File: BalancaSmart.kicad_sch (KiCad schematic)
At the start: 54 parts, among them J1 Load Cell, J2 Barrel_Jack, Q1 PMOS, Q2 NMOS, Q3 NMOS, Q4 S8050, SW1 SW_Push, U1 HX711-Mod, U2 ADS1115-module, U3 HX-2S-JH20, U4 XL4015

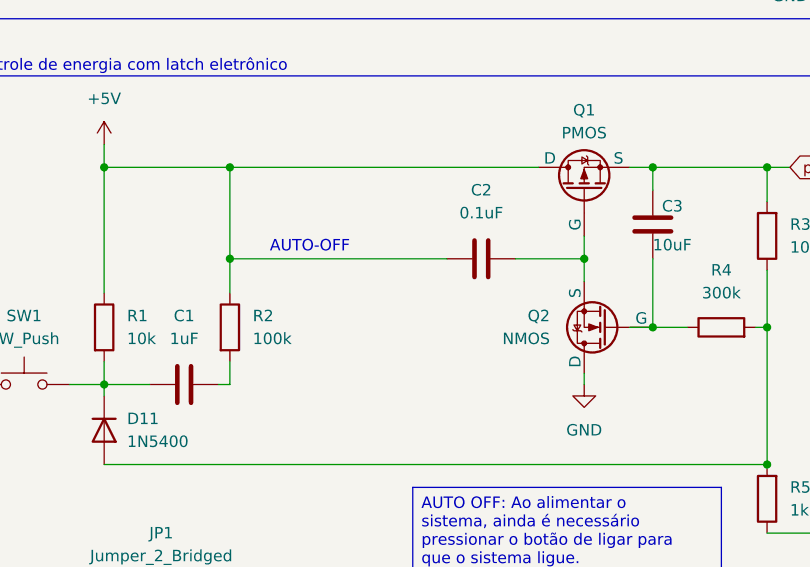
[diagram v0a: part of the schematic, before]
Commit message: correção na ligação do circuito de latch
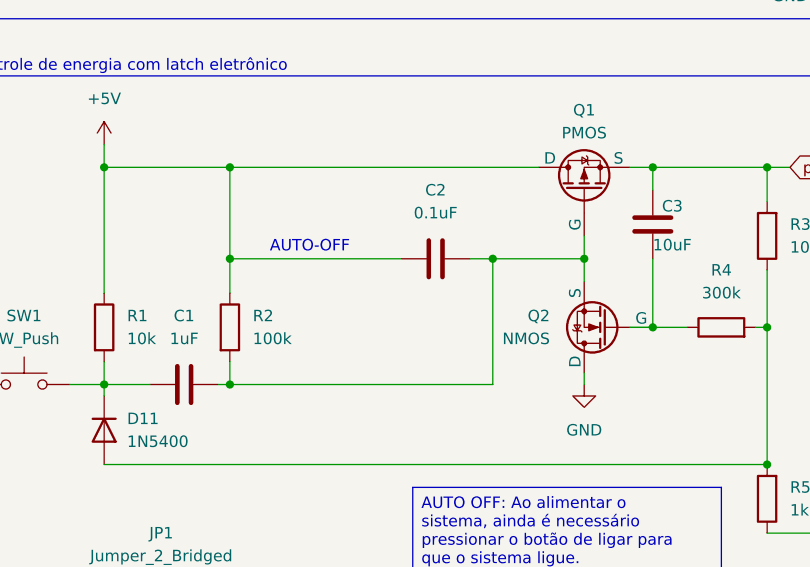
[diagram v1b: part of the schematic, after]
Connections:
- net at C2.2, Q1.2 (G), Q2.3 (S): now also C1.2, R2.2
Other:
- moved on the sheet: C2
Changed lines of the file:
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@@
 	)
 	(junction
+		(at 45.72 163.83)
+		(diameter 0)
+		(color 0 0 0 0)
+	)
+	(junction
 		(at 68.58 78.74)
 		(diameter 0)
@@
 	)
 	(junction
+		(at 74.93 149.86)
+		(diameter 0)
+		(color 0 0 0 0)
+	)
+	(junction
 		(at 200.66 27.94)
 		(diameter 0)
@@
 	(wire
 		(pts
+			(xy 45.72 163.83) (xy 74.93 163.83)
+		)
+		(stroke
+			(width 0)
+			(type default)
+		)
+	)
+	(wire
+		(pts
 			(xy 215.9 156.21) (xy 215.9 157.48)
 		)
@@
 	(wire
 		(pts
-			(xy 45.72 149.86) (xy 69.85 149.86)
+			(xy 45.72 149.86) (xy 64.77 149.86)
 		)
 		(stroke
@@
 	(wire
 		(pts
-			(xy 77.47 149.86) (xy 85.09 149.86)
-		)
-		(stroke
-			(width 0)
-			(type default)
-		)
-	)
-	(wire
-		(pts
 			(xy 219.71 41.91) (xy 219.71 46.99)
 		)
@@
 	(wire
 		(pts
+			(xy 72.39 149.86) (xy 74.93 149.86)
+		)
+		(stroke
+			(width 0)
+			(type default)
+		)
+	)
+	(wire
+		(pts
 			(xy 257.81 54.61) (xy 257.81 57.15)
 		)
@@
 	(wire
 		(pts
+			(xy 74.93 149.86) (xy 85.09 149.86)
+		)
+		(stroke
+			(width 0)
+			(type default)
+		)
+	)
+	(wire
+		(pts
 			(xy 250.19 57.15) (xy 257.81 57.15)
 		)
@@
 	(wire
 		(pts
+			(xy 74.93 163.83) (xy 74.93 149.86)
+		)
+		(stroke
+			(width 0)
+			(type default)
+		)
+	)
+	(wire
+		(pts
 			(xy 45.72 100.33) (xy 53.34 100.33)
 		)
@@
 	(symbol
 		(lib_id "Device:C")
-		(at 73.66 149.86 90)
+		(at 68.58 149.86 90)
 		(unit 1)
 		(body_style 1)
@@
 		(fields_autoplaced yes)
 		(property "Reference" "C2"
-			(at 73.66 142.24 90)
+			(at 68.58 142.24 90)
 			(show_name no)
 			(do_not_autoplace no)
@@
 		)
 		(property "Value" "0.1uF"
-			(at 73.66 144.78 90)
+			(at 68.58 144.78 90)
 			(show_name no)
 			(do_not_autoplace no)
@@
 		)
 		(property "Footprint" "Capacitor_THT:C_Disc_D5.0mm_W2.5mm_P2.50mm"
-			(at 77.47 148.8948 0)
+			(at 72.39 148.8948 0)
 			(hide yes)
 			(show_name no)
@@
 		)
 		(property "Datasheet" ""
-			(at 73.66 149.86 0)
+			(at 68.58 149.86 0)
 			(hide yes)
 			(show_name no)
@@
 		)
 		(property "Description" "Unpolarized capacitor"
-			(at 73.66 149.86 0)
+			(at 68.58 149.86 0)
 			(hide yes)
 			(show_name no)

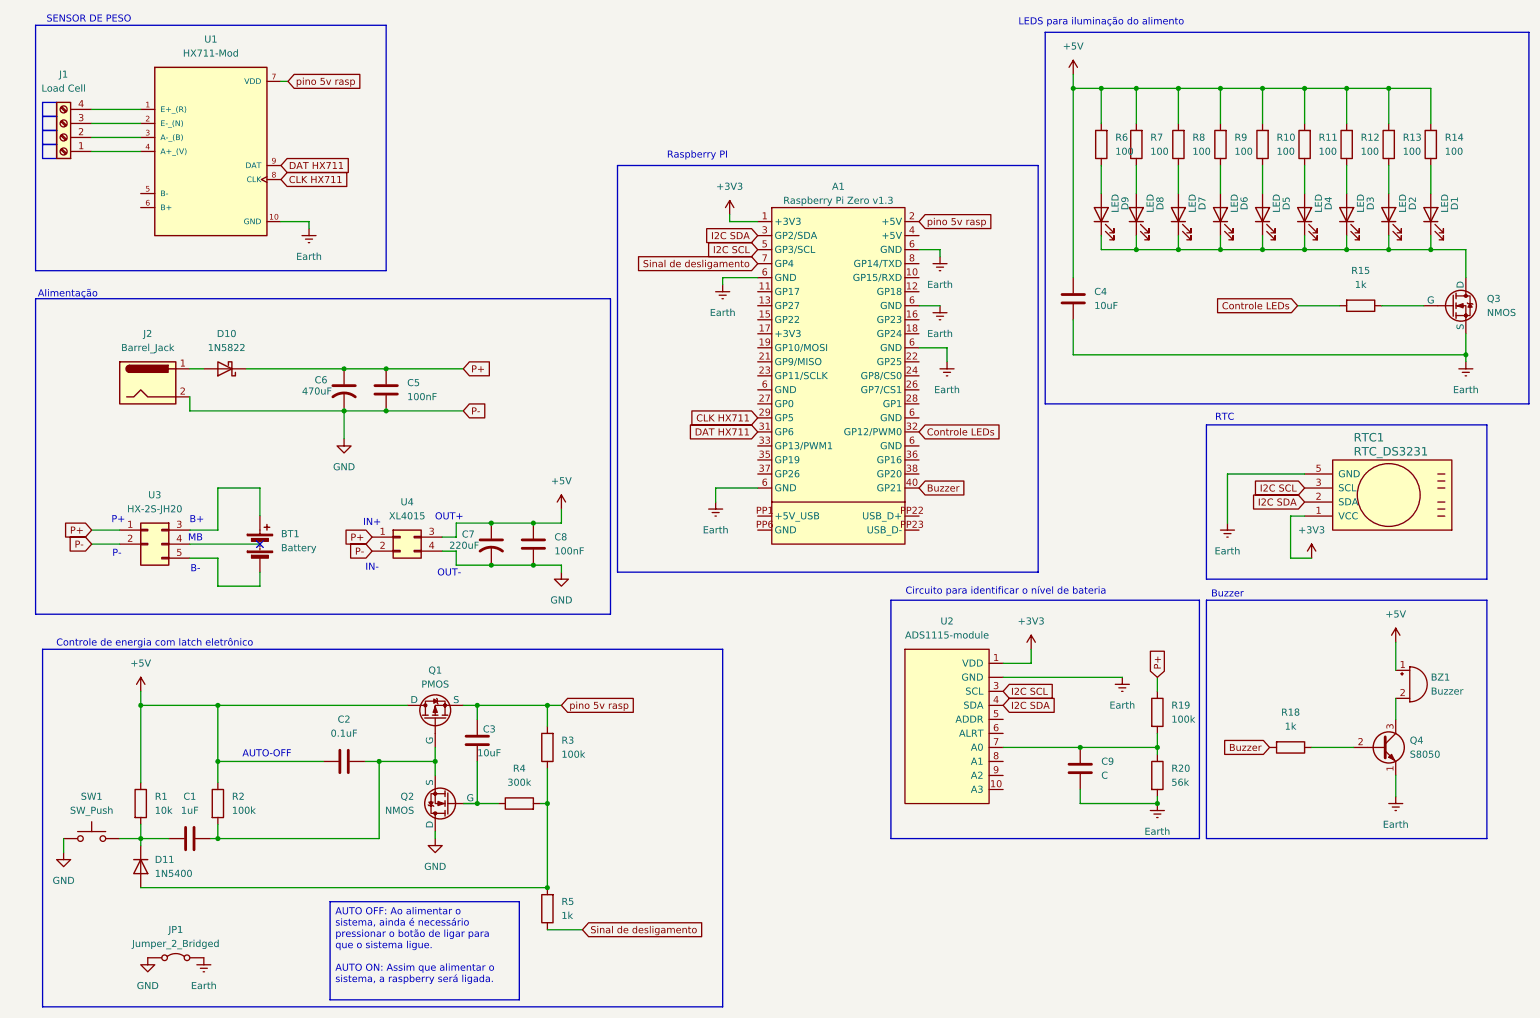
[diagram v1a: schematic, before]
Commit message: correção da orientação da raspberry e ADS1115 no layout da PCB e inicio do retrabalho do roteamento das trilhas
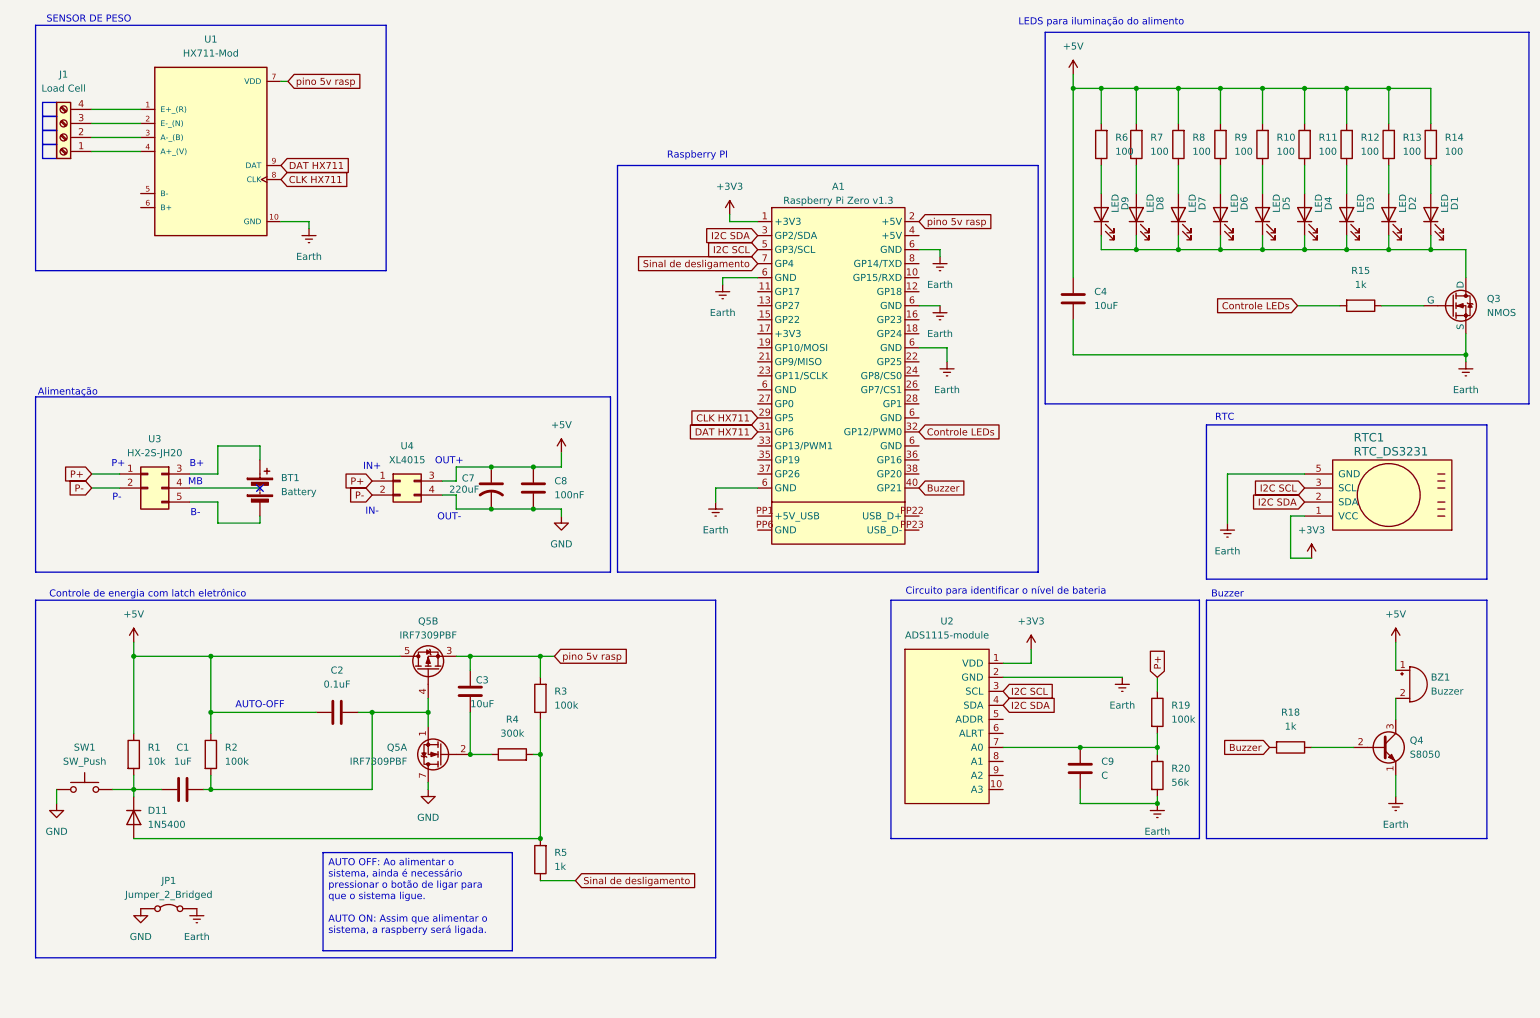
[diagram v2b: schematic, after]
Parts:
- removed C5: 100nF, Capacitor_THT:C_Disc_D5.0mm_W2.5mm_P2.50mm, symbol Device:C
- removed C6: 470uF, Capacitor_THT:C_Radial_D6.3mm_H7.0mm_P2.50mm, symbol Device:C_US
- removed D10: 1N5822, Diode_THT:D_DO-201AD_P15.24mm_Horizontal, symbol Diode:1N5822
- removed J2: Barrel_Jack, TerminalBlock:TerminalBlock_MaiXu_MX126-5.0-02P_1x02_P5.00mm, symbol Connector:Barrel_Jack
- removed Q1: PMOS, Package_TO_SOT_THT:TO-220-3_Vertical, symbol Simulation_SPICE:PMOS
- removed Q2: NMOS, Package_TO_SOT_THT:TO-220-3_Vertical, symbol Simulation_SPICE:NMOS
- added Q5: IRF7309PBF, Package_SO:SOIC-8_3.9x4.9mm_P1.27mm, symbol Transistor_FET:IRF7309PBF
- A1: footprint Raspberry_Pi_Zero_v.1.3_Hat:RASPI_ZERO_FULL -> Module:Raspberry_Pi_Zero_Socketed_THT_FaceDown_MountingHoles
- C1, C3: footprint Capacitor_THT:C_Radial_D6.3mm_H7.0mm_P2.50mm -> Capacitor_THT:C_Disc_D5.0mm_W2.5mm_P2.50mm
- U1: footprint HX711_mod:HX711_module -> project_library:HX711_module
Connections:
- net +5V: now also Q5.5 (D2), Q5.6 (D2)
- net Earth: now also U2.2 (GND); no longer U2.~ (GND)
- net GND: now also Q5.7 (D1), Q5.8 (D1); no longer U3.2 (P-), U4.2 (Pin_2)
- net pino 5v rasp: now also Q5.3 (S2)
- net at C3.1, R4.1: now also Q5.2 (G1)
- net at C1.2, C2.2, R2.2: now also Q5.1 (S1), Q5.4 (G2)
- new net P-: U3.2 (P-), U4.2 (Pin_2)
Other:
- moved on the sheet: BT1, C1, C2, C3, C7, C8, D11, JP1, R1, R2, R3, R4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
